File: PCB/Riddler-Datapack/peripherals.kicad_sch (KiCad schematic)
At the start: 0 parts

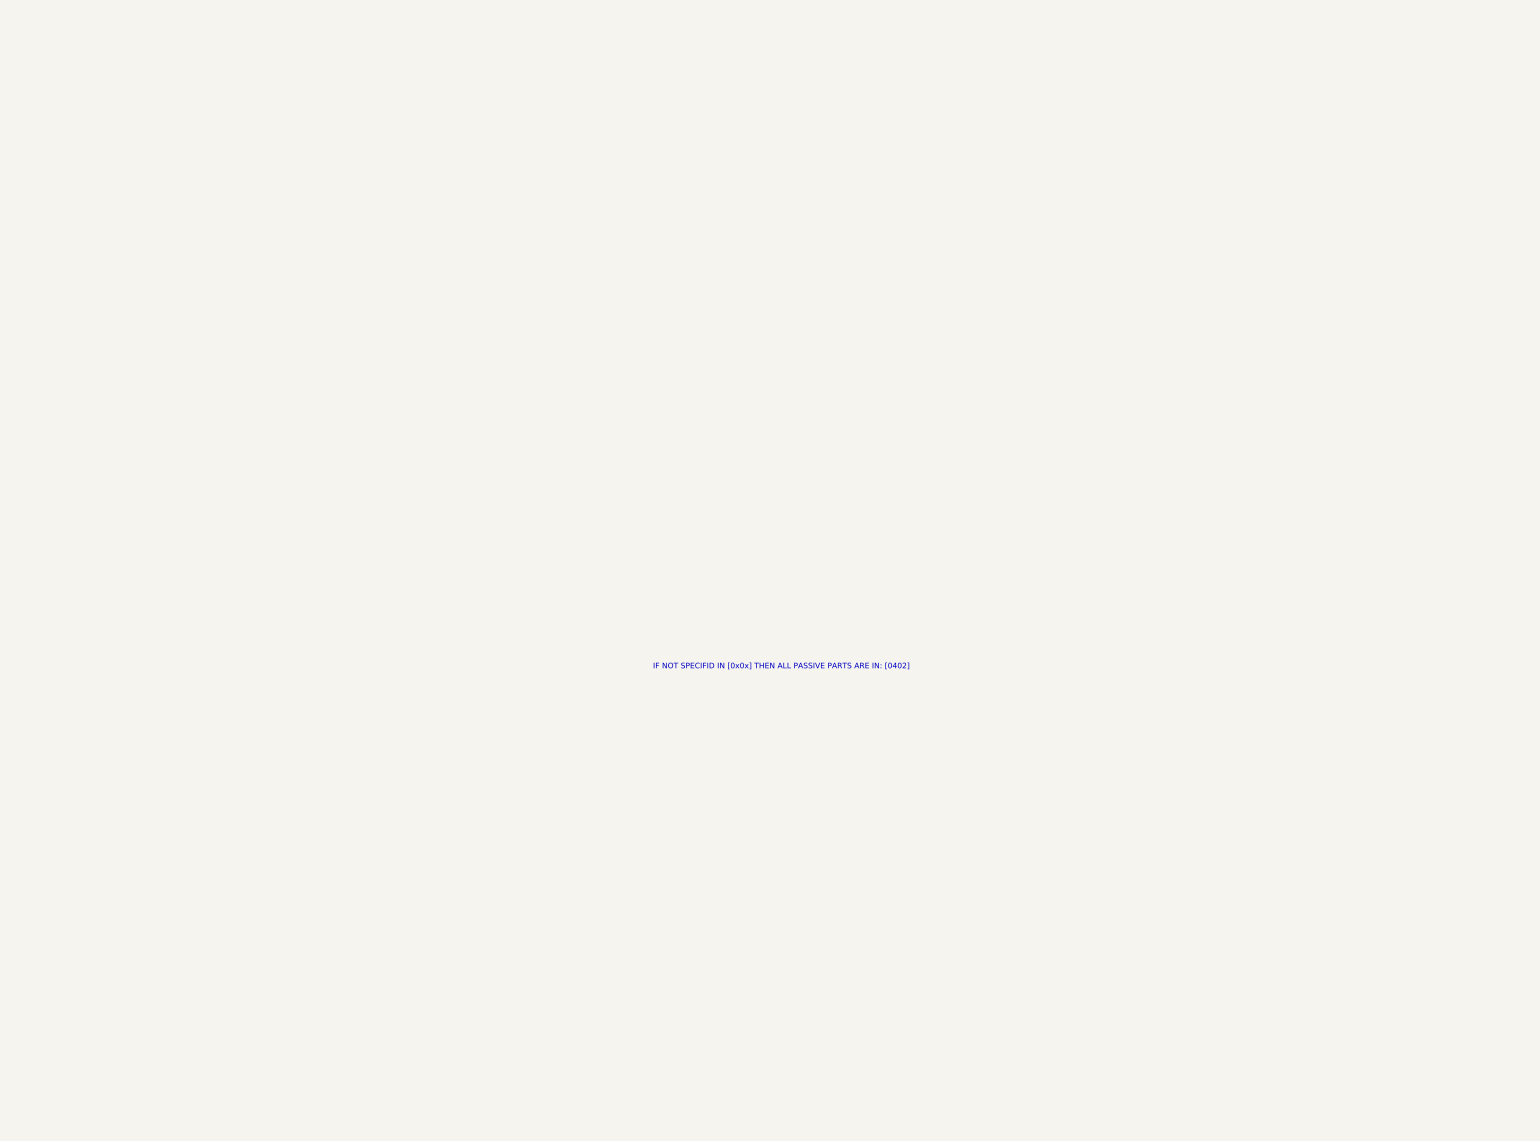
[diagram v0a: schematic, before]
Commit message: Complete schematics v0.5, add schematic PDF export and active prop reference
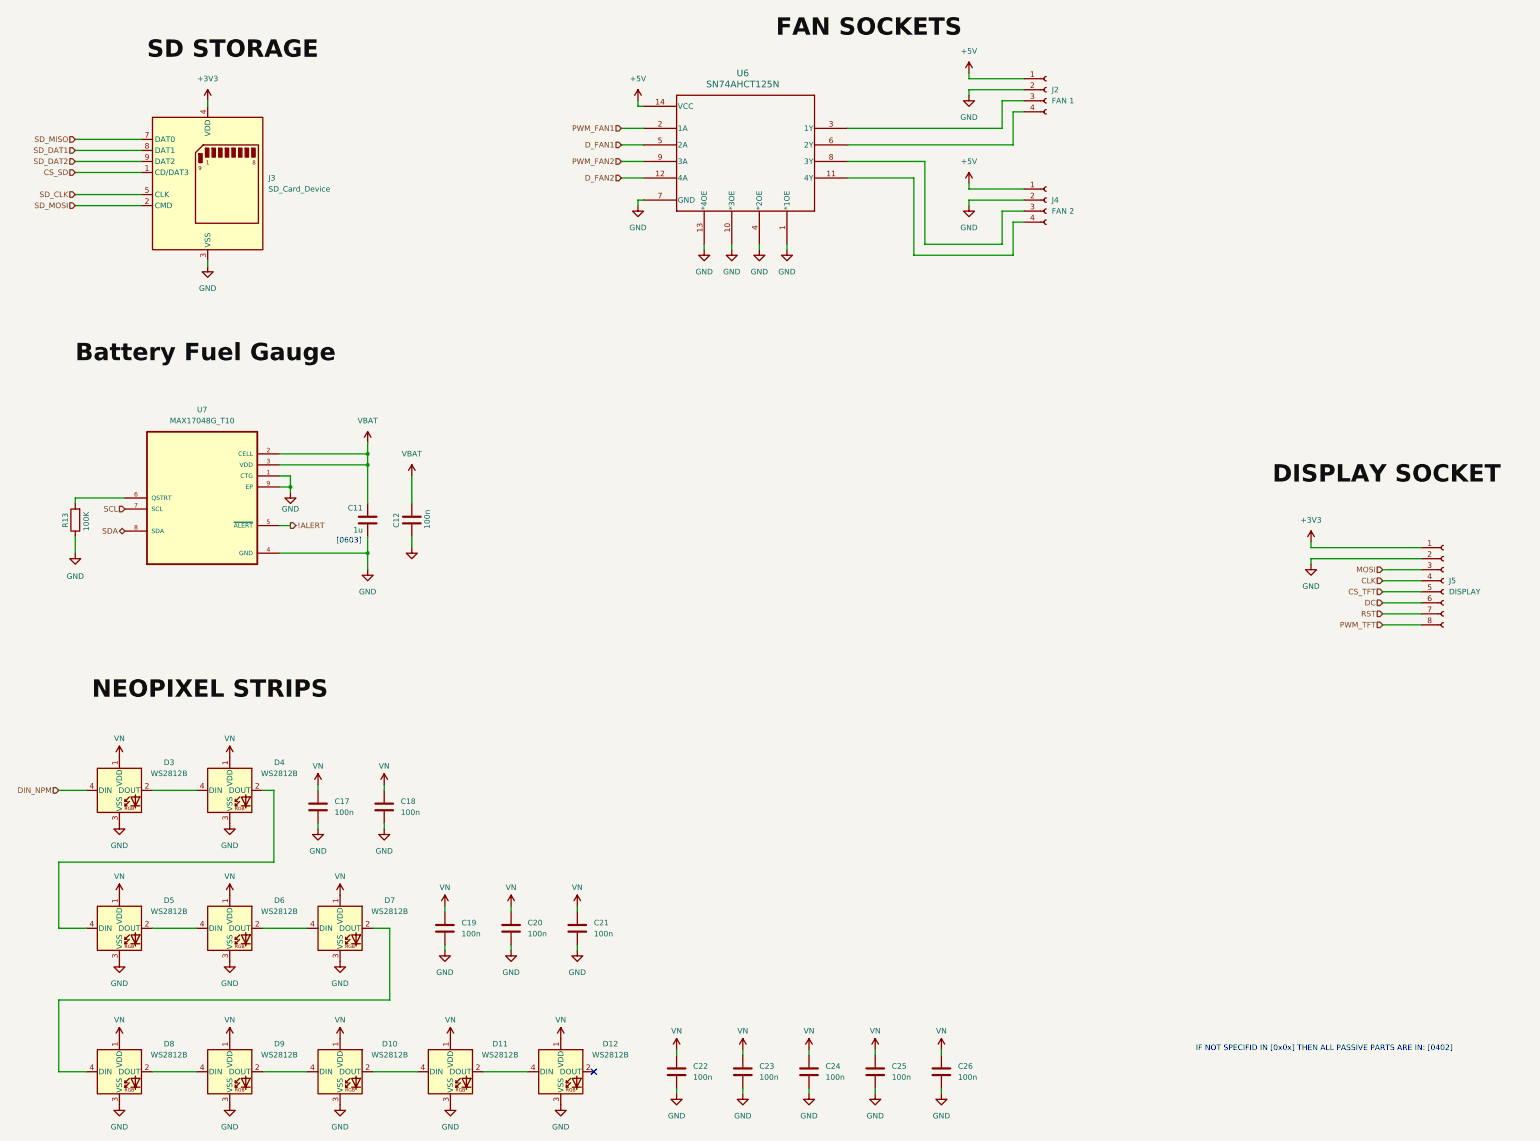
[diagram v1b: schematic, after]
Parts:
- added C11: 1u, Capacitor_SMD:C_0603_1608Metric, symbol Device:C
- added C12, C17, C18, C19, C20, C21, C22, C23, C24, C25, C26: 100n, Capacitor_SMD:C_0402_1005Metric, symbol Device:C
- added D10, D11, D12, D3, D4, D5, D6, D7, D8, D9: WS2812B, LED_SMD:LED_WS2812B_PLCC4_5.0x5.0mm_P3.2mm, symbol LED:WS2812B
- added J2: FAN 1, Connector_PinHeader_2.54mm:PinHeader_1x04_P2.54mm_Vertical, symbol Connector:Conn_01x04_Socket
- added J3: SD_Card_Device, Connector_Card:SD_Card_Device_16mm_SlotDepth, symbol Connector:SD_Card_Device
- added J4: FAN 2, Connector_PinHeader_2.54mm:PinHeader_1x04_P2.54mm_Vertical, symbol Connector:Conn_01x04_Socket
- added J5: DISPLAY, Connector_JST:JST_PH_B8B-PH-K_1x08_P2.00mm_Vertical, symbol Connector:Conn_01x08_Socket
- added R13: 100K, Resistor_SMD:R_0402_1005Metric, symbol Device:R
- added U6: SN74AHCT125N, foot:N14, symbol SN74AHCT125N:SN74AHCT125N
- added U7: MAX17048G_T10, Global Footprints:SON50P200X200X80-9N, symbol MAX17048G_T10:MAX17048G_T10
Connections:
- new net: J2.3 (Pin_3), U6.3 (1Y)
- new net: J2.4 (Pin_4), U6.6 (2Y)
- new net: D11.2 (DOUT), D12.4 (DIN)
- new net: D10.2 (DOUT), D11.4 (DIN)
- new net: R13.2, U7.6 (QSTRT)
- new net: D8.2 (DOUT), D9.4 (DIN)
- new net: D7.2 (DOUT), D8.4 (DIN)
- new net: J4.3 (Pin_3), U6.8 (3Y)
- new net: J4.4 (Pin_4), U6.11 (4Y)
- new net: D3.2 (DOUT), D4.4 (DIN)
- new net: D5.2 (DOUT), D6.4 (DIN)
- new net: D4.2 (DOUT), D5.4 (DIN)
- new net: D10.4 (DIN), D9.2 (DOUT)
- new net: D6.2 (DOUT), D7.4 (DIN)
- new net !ALERT: U7.5 (~{ALERT})
- new net +3V3: J3.4 (VDD), J5.1 (Pin_1)
- new net +5V: J2.1 (Pin_1), J4.1 (Pin_1), U6.14 (VCC)
- new net CLK: J5.4 (Pin_4)
- new net CS_SD: J3.1 (CD/DAT3)
- new net CS_TFT: J5.5 (Pin_5)
- new net DC: J5.6 (Pin_6)
- new net DIN_NPM: D3.4 (DIN)
- new net D_FAN1: U6.5 (2A)
- new net D_FAN2: U6.12 (4A)
- new net GND: C11.2, C12.2, C17.2, C18.2, C19.2, C20.2, C21.2, C22.2, C23.2, C24.2, C25.2, C26.2, D10.3 (VSS), D11.3 (VSS), D12.3 (VSS), D3.3 (VSS), D4.3 (VSS), D5.3 (VSS), D6.3 (VSS), D7.3 (VSS), D8.3 (VSS), D9.3 (VSS), J2.2 (Pin_2), J3.3 (VSS), J3.6 (VSS), J4.2 (Pin_2), J5.2 (Pin_2), R13.1, U6.1 (*1OE), U6.10 (*3OE), U6.13 (*4OE), U6.4 (*2OE), U6.7 (GND), U7.1 (CTG), U7.4 (GND), U7.9 (EP)
- new net MOSI: J5.3 (Pin_3)
- new net PWM_FAN1: U6.2 (1A)
- new net PWM_FAN2: U6.9 (3A)
- new net PWM_TFT: J5.8 (Pin_8)
- new net RST: J5.7 (Pin_7)
- new net SCL: U7.7 (SCL)
- new net SDA: U7.8 (SDA)
- new net SD_CLK: J3.5 (CLK)
- new net SD_DAT1: J3.8 (DAT1)
- new net SD_DAT2: J3.9 (DAT2)
- new net SD_MISO: J3.7 (DAT0)
- new net SD_MOSI: J3.2 (CMD)
- new net VBAT: C11.1, C12.1, U7.2 (CELL), U7.3 (VDD)
- new net VN: C17.1, C18.1, C19.1, C20.1, C21.1, C22.1, C23.1, C24.1, C25.1, C26.1, D10.1 (VDD), D11.1 (VDD), D12.1 (VDD), D3.1 (VDD), D4.1 (VDD), D5.1 (VDD), D6.1 (VDD), D7.1 (VDD), D8.1 (VDD), D9.1 (VDD)
- no-connect marks 0 -> 1
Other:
- note added: "[0603]"
